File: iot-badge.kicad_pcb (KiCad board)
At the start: 2 copper layers, 100 x 70 mm, 16 parts, among them J1 USB_C_Receptacle_USB2.0, J11 Conn_01x01_Male, J12 Conn_01x01_Male, SW1 SW_Push, SW2 SW_Push, SW3 SW_Push, SW4 SW_Push, SW5 SW_Push, SW6 SW_Push, U1 ESP32-WROOM-32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

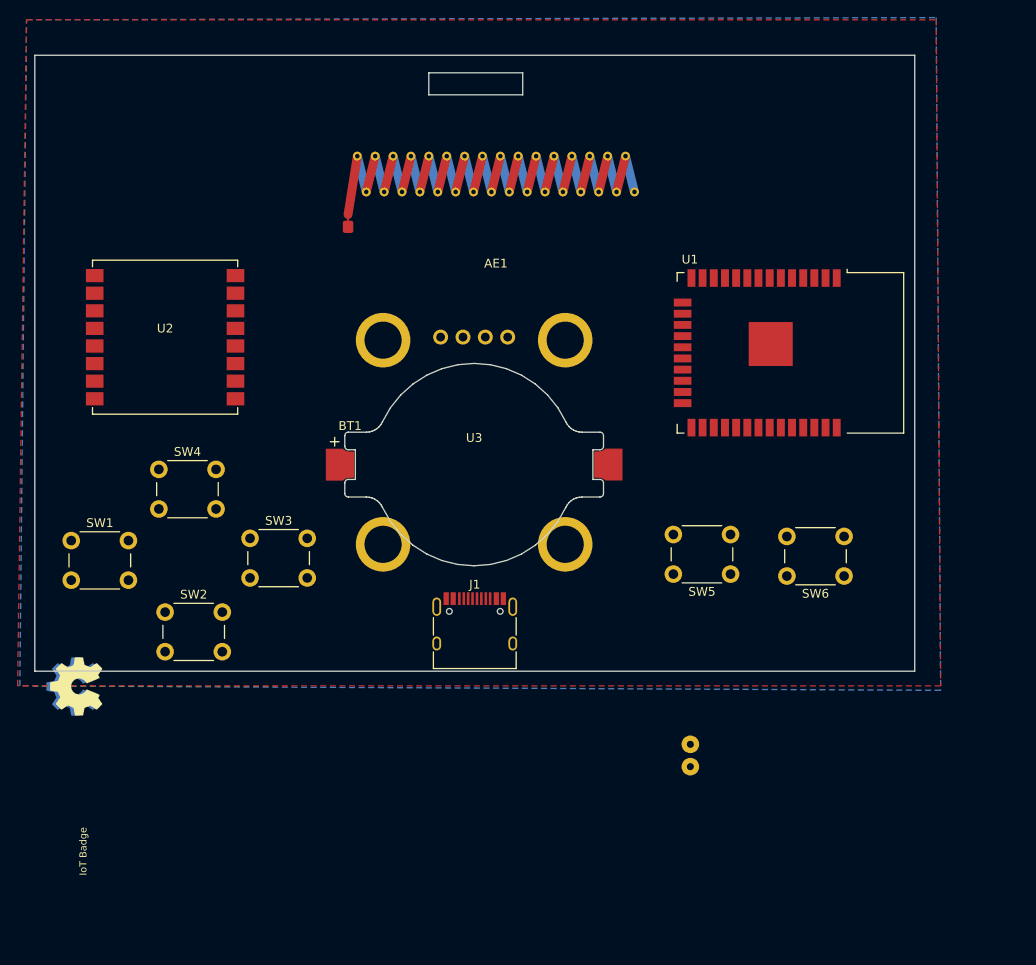
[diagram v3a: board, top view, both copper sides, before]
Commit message: improved holding holes
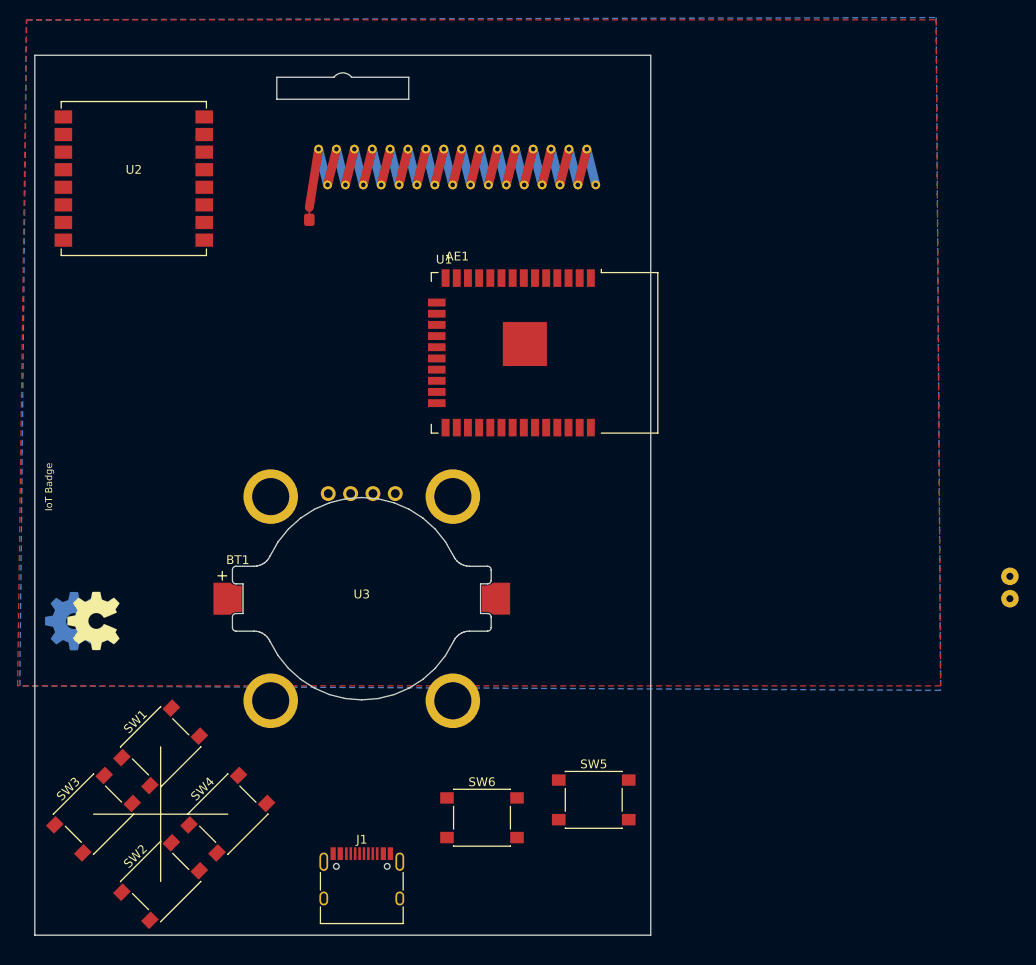
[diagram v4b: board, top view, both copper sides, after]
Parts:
- SW1, SW2, SW3, SW4, SW5, SW6: footprint Button_Switch_THT:SW_PUSH_6mm -> Button_Switch_SMD:SW_Push_1P1T_NO_6x6mm_H9.5mm
- moved SW6 49.5 mm to (150.8, 136.7), turned to 0 degrees
- moved J11 41.0 mm to (210.8, 109.2)
- moved J12 41.0 mm to (210.8, 111.8)
- moved SW4 40.0 mm to (121.9, 136.2), turned to 45 degrees
- moved SW3 36.0 mm to (106.7, 136.2), turned to 45 degrees
- moved J1 31.7 mm to (137.2, 144.8)
- moved SW2 30.6 mm to (114.3, 143.9), turned to 45 degrees
- moved SW5 30.0 mm to (163.5, 134.6), turned to 0 degrees
- moved U1 27.9 mm to (154.9, 83.8)
- moved SW1 25.6 mm to (114.3, 128.6), turned to 45 degrees
- moved U3 21.9 mm to (137.2, 111.8)
- moved BT1 19.9 mm to (137.2, 111.8)
- moved U2 18.4 mm to (111.3, 64.0)
- moved REF** 7.69 mm to (106.7, 114.3)
- moved REF** 7.44 mm to (104.1, 114.3)
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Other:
- board size 100 x 70 mm -> 70 x 100 mm

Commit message: changed battery for AAA
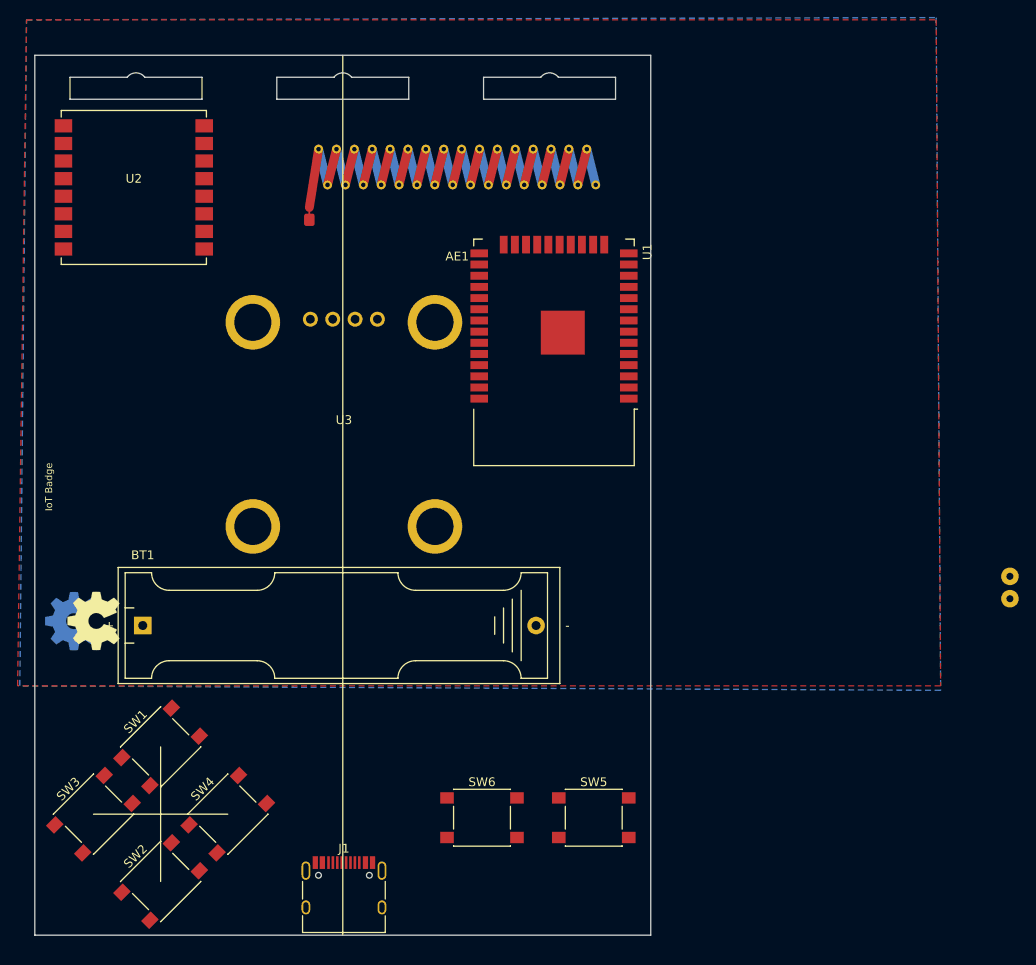
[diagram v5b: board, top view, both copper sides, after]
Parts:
- BT1: footprint Battery:BatteryHolder_Keystone_1057_1x2032 -> Battery:BatteryHolder_Keystone_2466_1xAAA
- moved BT1 25.1 mm to (112.3, 114.8)
- moved U3 19.9 mm to (135.1, 91.9)
- moved U1 5.08 mm to (159.0, 80.8), turned to 180 degrees
- moved J1 2.27 mm to (135.1, 145.8)
- moved SW5 2.03 mm to (163.5, 136.7)
- moved U2 1.02 mm to (111.3, 65.0)
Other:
- outline, holes or cut-outs redrawn

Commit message: added some USB components
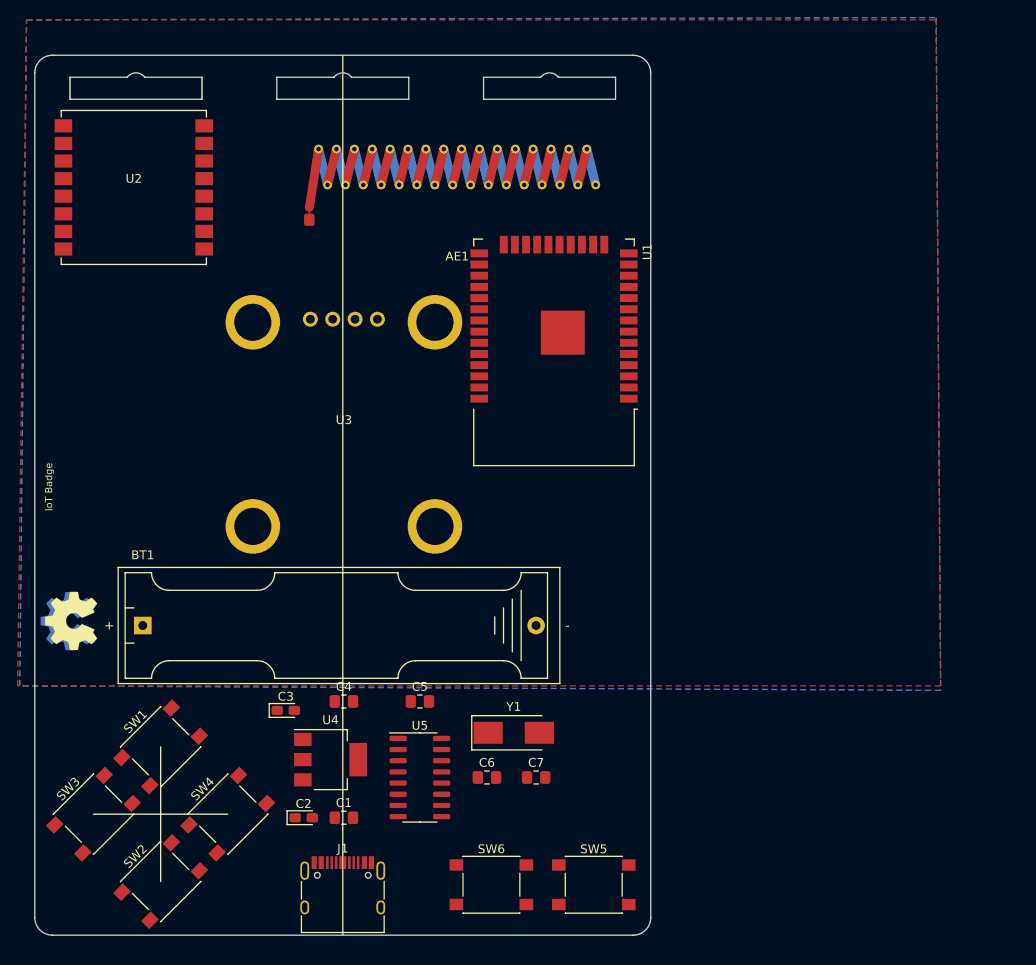
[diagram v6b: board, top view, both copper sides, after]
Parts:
- removed J11, J12: Conn_01x01_Male, Connector_Wire:SolderWirePad_1x01_Drill0.8mm
- added C1: 100nF, Capacitor_SMD:C_0805_2012Metric_Pad1.18x1.45mm_HandSolder, F.Cu at (135.1, 136.7)
- added C2: 22uF, Capacitor_Tantalum_SMD:CP_EIA-2012-15_AVX-P_Pad1.30x1.05mm_HandSolder, F.Cu at (130.6, 136.7)
- added C3: 22uF, Capacitor_Tantalum_SMD:CP_EIA-2012-15_AVX-P_Pad1.30x1.05mm_HandSolder, F.Cu at (128.5, 124.5)
- added C4: 100nF, Capacitor_SMD:C_0805_2012Metric_Pad1.18x1.45mm_HandSolder, F.Cu at (135.1, 123.4)
- added C5: 100nF, Capacitor_SMD:C_0805_2012Metric_Pad1.18x1.45mm_HandSolder, F.Cu at (143.8, 123.4)
- added C6: 22pF, Capacitor_SMD:C_0805_2012Metric_Pad1.18x1.45mm_HandSolder, F.Cu at (151.4, 132.1)
- added C7: 22pF, Capacitor_SMD:C_0805_2012Metric_Pad1.18x1.45mm_HandSolder, F.Cu at (157.0, 132.1)
- added U4: AMS1117-3.3, Package_TO_SOT_SMD:SOT-223-3_TabPin2, F.Cu at (133.6, 130.0)
- added U5: CH340G, Package_SO:SOIC-16_3.9x9.9mm_P1.27mm, F.Cu at (143.8, 132.1)
- added Y1: Crystal, Crystal:Crystal_SMD_0603-2Pin_6.0x3.5mm_HandSoldering, F.Cu at (154.4, 127.0)
- moved SW6 7.69 mm to (151.9, 144.3)
- moved SW5 7.62 mm to (163.5, 144.3)
- moved REF** 2.54 mm to (104.1, 114.3)
- moved REF** 0.51 mm to (103.6, 114.3)
- moved J1 0.13 mm to (135.0, 145.8)
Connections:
- net Net-(J1-PadA1) renamed Earth
- J1 pad A6: unconnected-(J1-PadA6) -> Net-(J1-PadA6)
- J1 pad A7: unconnected-(J1-PadA7) -> Net-(J1-PadA7)
- J1 pad B6: unconnected-(J1-PadB6) -> Net-(J1-PadA6)
- J1 pad B7: unconnected-(J1-PadB7) -> Net-(J1-PadA7)
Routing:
- added copper zone on B.Cu, net (none)
- added copper zone on F.Cu, net (none)
- removed copper zone on B.Cu, net Net-(J11-Pad1)
- removed copper zone on F.Cu, net Net-(J11-Pad1)
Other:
- outline, holes or cut-outs redrawn

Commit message: ant needs some care NETS
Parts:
- added C8: 100nF, Capacitor_SMD:C_0805_2012Metric_Pad1.18x1.45mm_HandSolder, F.Cu at (140.7, 88.4)
- added Q1: BC847, Package_TO_SOT_SMD:SOT-23, F.Cu at (167.1, 127.5)
- added Q2: BC847, Package_TO_SOT_SMD:SOT-23, F.Cu at (167.1, 133.1)
- added R1: 10k, Resistor_SMD:R_0805_2012Metric_Pad1.20x1.40mm_HandSolder, F.Cu at (145.5, 88.4)
- added R2: 10k, Resistor_SMD:R_0805_2012Metric_Pad1.20x1.40mm_HandSolder, F.Cu at (162.6, 128.0)
- added R3: 10k, Resistor_SMD:R_0805_2012Metric_Pad1.20x1.40mm_HandSolder, F.Cu at (162.6, 133.1)
- AE1: value Antenna -> Antenna 433
- moved AE1 0.40 mm to (148.3, 62.5)
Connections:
- AE1 pad 1: unconnected-(AE1-Pad1) -> Net-(AE1-Pad1)
- U1 pad 1: Net-(U1-Pad1) -> Earth
- U1 pad 15: Net-(U1-Pad1) -> Earth
- U1 pad 2: unconnected-(U1-Pad2) -> +3V3
- U1 pad 25: unconnected-(U1-Pad25) -> /IO0
- U1 pad 3: unconnected-(U1-Pad3) -> /EN
- U1 pad 38: Net-(U1-Pad1) -> Earth
- U1 pad 39: Net-(U1-Pad1) -> Earth
- U2 pad 14: unconnected-(U2-Pad14) -> Net-(AE1-Pad1)
- U5 pad 13: unconnected-(U5-Pad13) -> /IO0
- U5 pad 14: unconnected-(U5-Pad14) -> Net-(U5-Pad14)

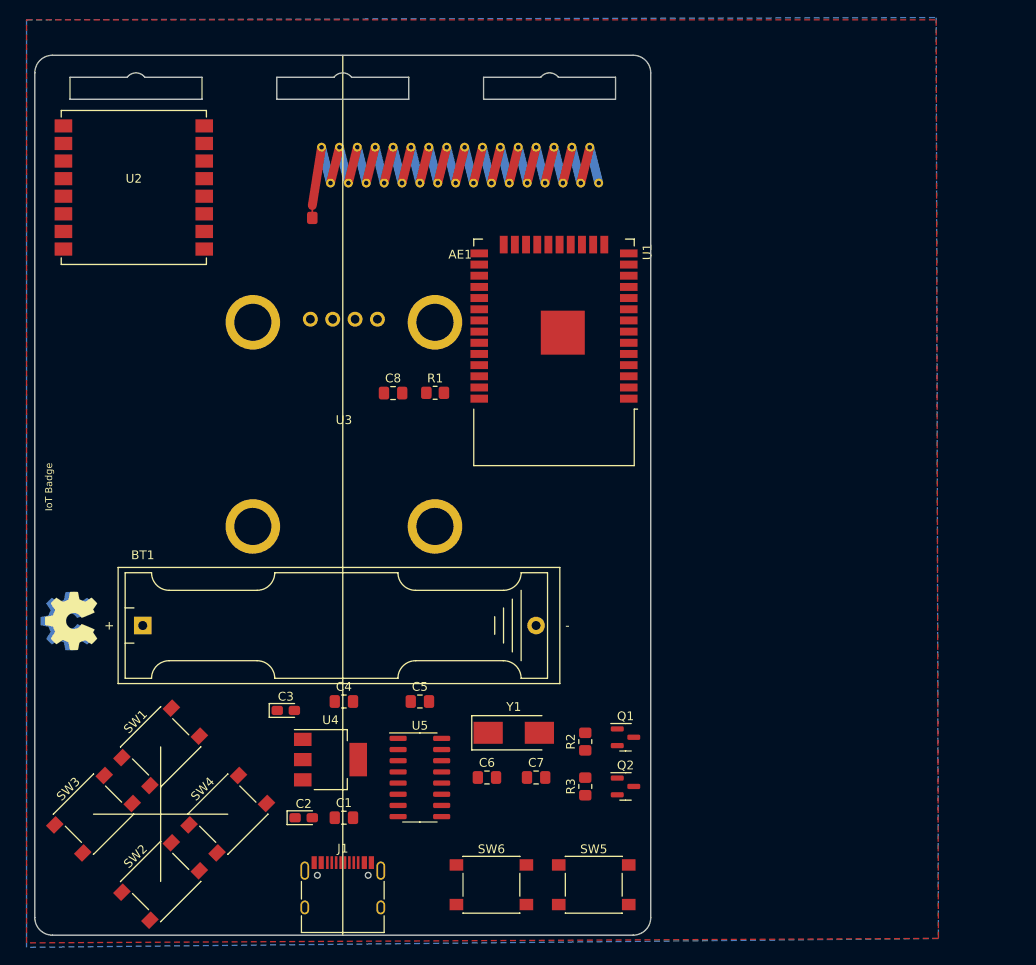
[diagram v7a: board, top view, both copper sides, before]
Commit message: ant needs routing rules
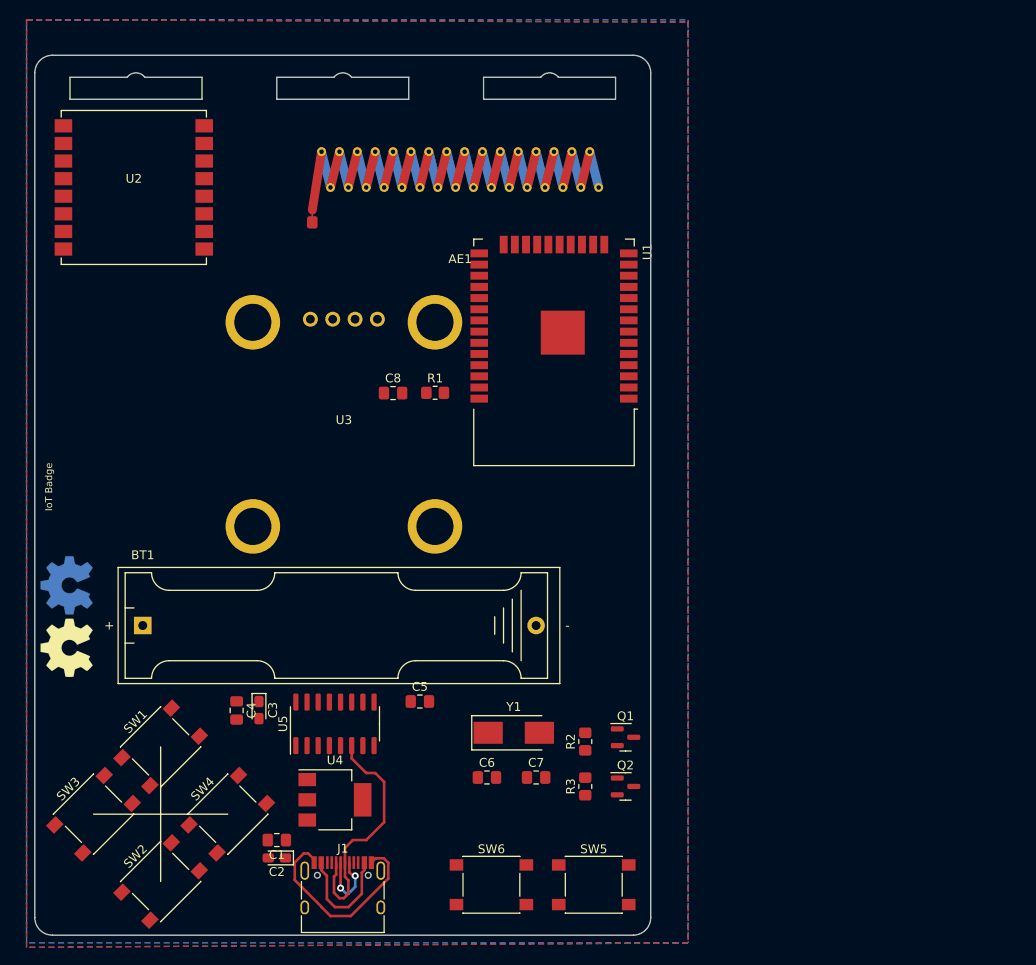
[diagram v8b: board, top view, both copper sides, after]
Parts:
- moved C4 12.2 mm to (122.9, 124.5), turned to -90 degrees
- moved U5 11.4 mm to (134.1, 126.0), turned to 90 degrees
- moved C1 8.03 mm to (127.5, 139.2), turned to 180 degrees
- moved C2 5.49 mm to (127.5, 141.2), turned to 180 degrees
- moved U4 4.60 mm to (134.1, 134.6)
- moved SYMB1 4.06 mm to (103.6, 110.2)
- moved SYMB2 3.09 mm to (103.6, 117.3)
- moved C3 3.05 mm to (125.5, 124.4), turned to -90 degrees
- moved AE1 0.51 mm to (148.3, 63.0)
- renumbered REF** to SYMB1, REF** to SYMB2
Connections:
- AE1 pad 10: (no net) -> Net-(AE1-Pad1)
- AE1 pad 11: (no net) -> Net-(AE1-Pad1)
- AE1 pad 12: (no net) -> Net-(AE1-Pad1)
- AE1 pad 13: (no net) -> Net-(AE1-Pad1)
- AE1 pad 14: (no net) -> Net-(AE1-Pad1)
- AE1 pad 15: (no net) -> Net-(AE1-Pad1)
- AE1 pad 16: (no net) -> Net-(AE1-Pad1)
- AE1 pad 17: (no net) -> Net-(AE1-Pad1)
- AE1 pad 18: (no net) -> Net-(AE1-Pad1)
- AE1 pad 19: (no net) -> Net-(AE1-Pad1)
- AE1 pad 20: (no net) -> Net-(AE1-Pad1)
- AE1 pad 21: (no net) -> Net-(AE1-Pad1)
- AE1 pad 22: (no net) -> Net-(AE1-Pad1)
- AE1 pad 23: (no net) -> Net-(AE1-Pad1)
- AE1 pad 24: (no net) -> Net-(AE1-Pad1)
- AE1 pad 25: (no net) -> Net-(AE1-Pad1)
- AE1 pad 26: (no net) -> Net-(AE1-Pad1)
- AE1 pad 27: (no net) -> Net-(AE1-Pad1)
- AE1 pad 28: (no net) -> Net-(AE1-Pad1)
- AE1 pad 29: (no net) -> Net-(AE1-Pad1)
- AE1 pad 30: (no net) -> Net-(AE1-Pad1)
- AE1 pad 31: (no net) -> Net-(AE1-Pad1)
- AE1 pad 32: (no net) -> Net-(AE1-Pad1)
- AE1 pad 33: (no net) -> Net-(AE1-Pad1)
- AE1 pad 8: (no net) -> Net-(AE1-Pad1)
- AE1 pad 9: (no net) -> Net-(AE1-Pad1)
- U2 pad 1: Net-(U2-Pad1) -> unconnected-(U2-Pad1)
- U2 pad 16: Net-(U2-Pad1) -> unconnected-(U2-Pad1)
- U2 pad 2: Net-(U2-Pad1) -> unconnected-(U2-Pad1)
- U2 pad 9: Net-(U2-Pad1) -> unconnected-(U2-Pad1)
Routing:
- net Net-(J1-PadA7): track 0.00 -> 27.5 mm
- net Earth: track 0.00 -> 23.5 mm
- net Net-(C1-Pad1): track 0.00 -> 13.1 mm
- net Net-(J1-PadA6): track 0.00 -> 8.34 mm, vias 0 -> 2
- added copper zone on B.Cu, net Earth
- added copper zone on F.Cu, net Earth
- removed copper zone on B.Cu, net (none)
- removed copper zone on F.Cu, net (none)
